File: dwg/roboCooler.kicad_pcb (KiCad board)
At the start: 2 copper layers, 139.7 x 137.2 mm, 44 parts, among them J1 CONN_02X25, J10 CONN_01X12, J11 CONN_01X12, J2 CONN_02X25, J3 CONN_01X04, J5 CONN_01X02, J7 CONN_01X02, J9 CONN_01X06, Q1 NMOS, Q2 NMOS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

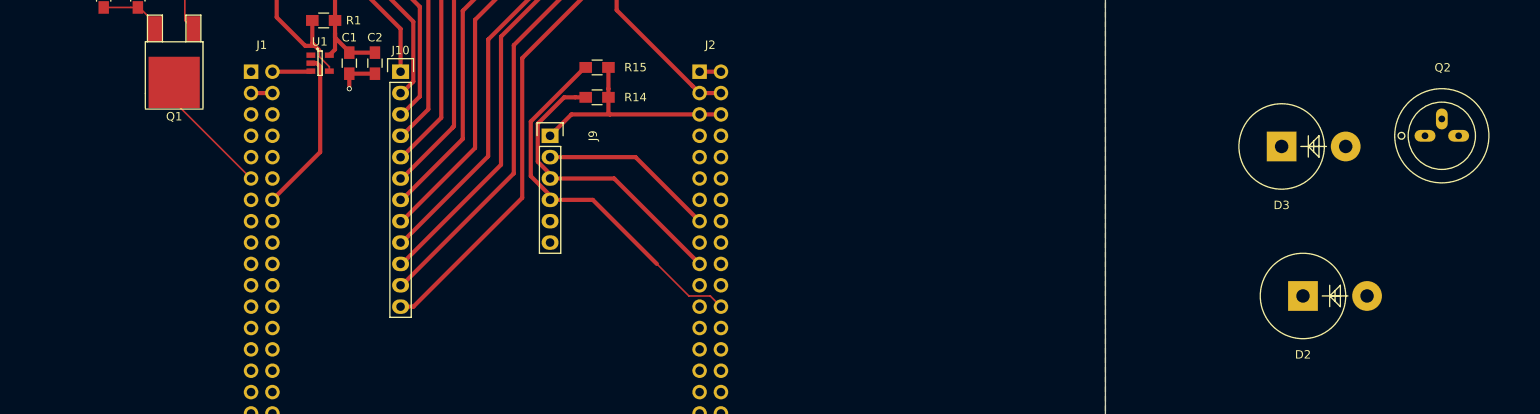
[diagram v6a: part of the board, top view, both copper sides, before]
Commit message: added pump parts to layout
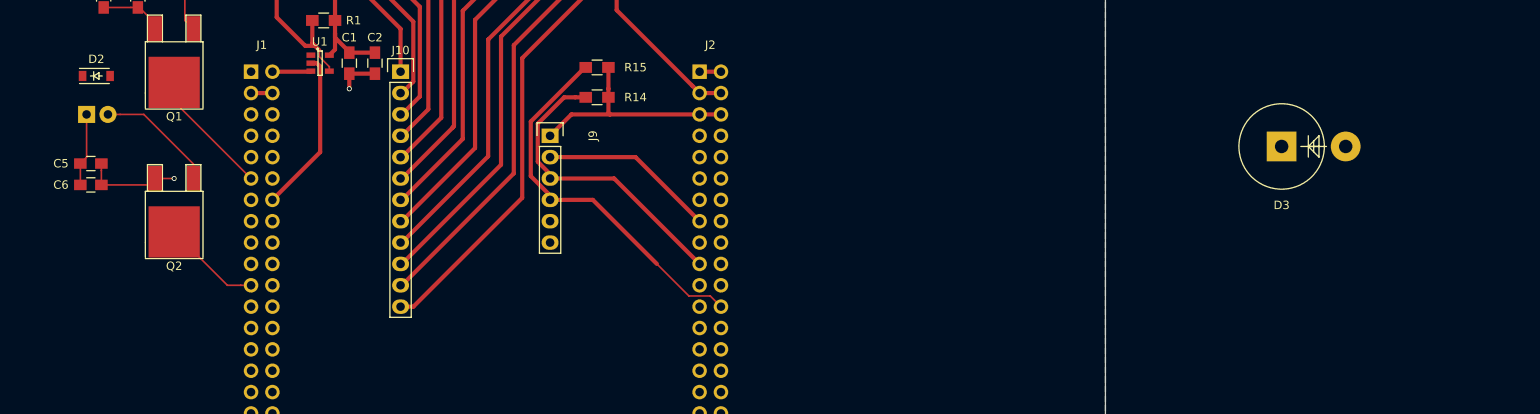
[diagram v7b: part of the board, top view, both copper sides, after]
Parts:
- added C5: .01UF, Capacitors_SMD:C_0805_HandSoldering, F.Cu at (44.5, 51.6)
- added C6: 1UF, Capacitors_SMD:C_0805_HandSoldering, F.Cu at (44.5, 54.1)
- added J4: CONN_01X02, Socket_Strips:Socket_Strip_Angled_1x02, B.Cu at (43.9, 45.7)
- D2: value D_Schottky_Small -> BAT42; footprint Diodes_ThroughHole:Diode_P600_Vertical_AnodeUp -> Diodes_SMD:SOD-123
- Q2: footprint Transistors_OldSowjetAera:OldSowjetaera_Transistor_Type-II_BigPads -> TO_SOT_Packages_SMD:TO-252-2Lead
- moved Q2 150.8 mm to (54.4, 53.3), turned to 180 degrees
- moved D2 145.9 mm to (45.1, 41.1)
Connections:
- J1 pad 21: Net-(J1-Pad21) -> PUMP
- J2 pad 25: PUMP -> Net-(J2-Pad25)
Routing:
- net Net-(D2-Pad2): track 0.00 -> 14.3 mm
- net PUMP: track 0.00 -> 12.7 mm
- net POWER_GND: track 19.8 -> 31.3 mm, vias 1 -> 2
- net +12V: track 11.3 -> 20.0 mm

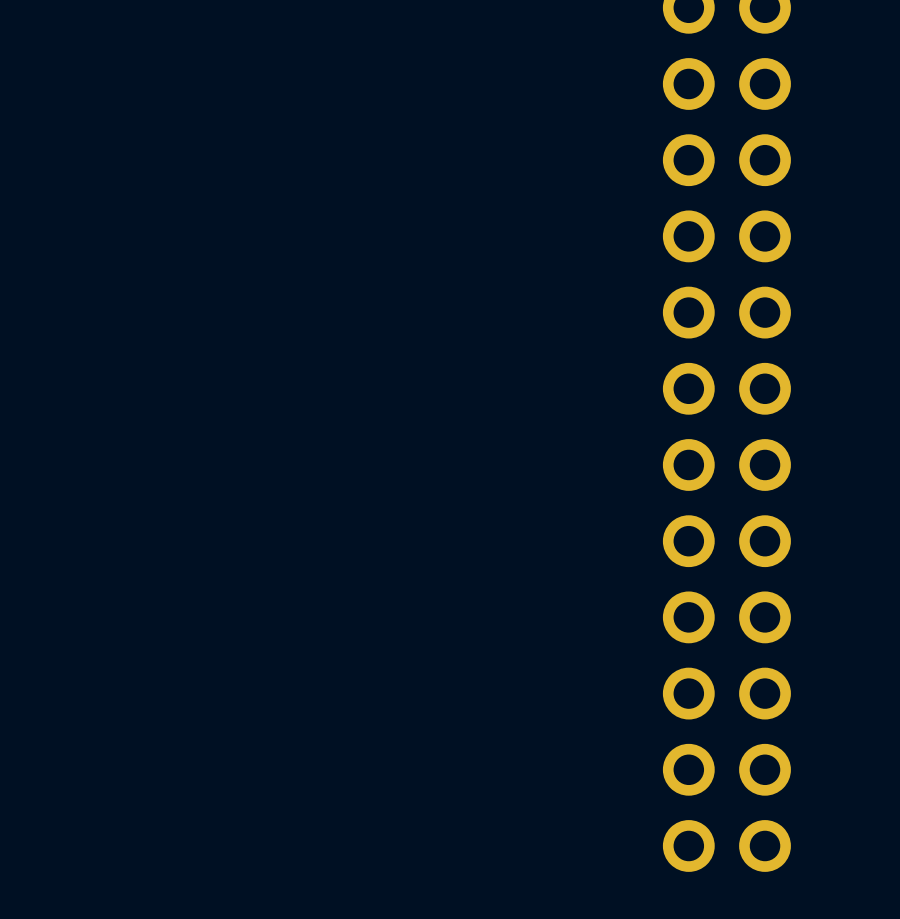
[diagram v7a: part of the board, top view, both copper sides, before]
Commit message: added hall sensors to layout
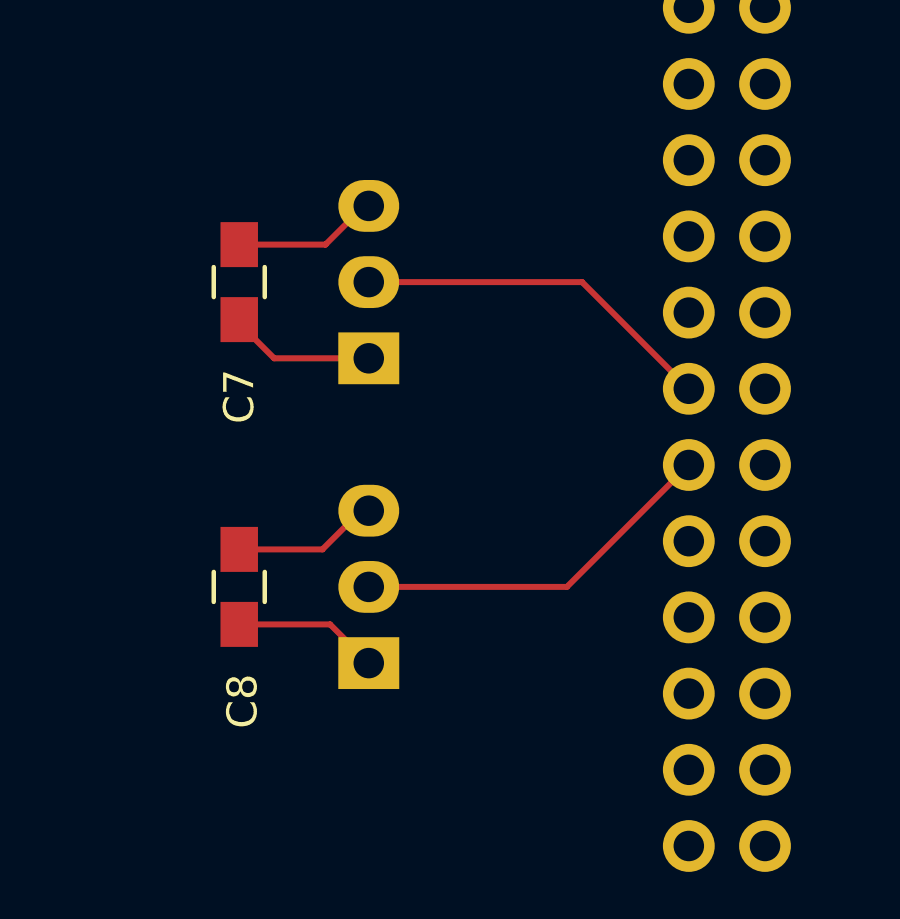
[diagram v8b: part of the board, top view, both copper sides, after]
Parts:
- added C7: .1UF, Capacitors_SMD:C_0805_HandSoldering, F.Cu at (48.5, 82.8)
- added C8: .1UF, Capacitors_SMD:C_0805_HandSoldering, F.Cu at (48.5, 93.0)
- added P1: CONN_01X03, Socket_Strips:Socket_Strip_Angled_1x03, B.Cu at (52.8, 85.3)
- added P2: CONN_01X03, Socket_Strips:Socket_Strip_Angled_1x03, B.Cu at (52.8, 95.5)
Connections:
- J1 pad 35: HALL_1 -> Net-(J1-Pad35)
- J1 pad 36: HALL_2 -> Net-(J1-Pad36)
- J1 pad 37: Net-(J1-Pad37) -> HALL_1
- J1 pad 39: Net-(J1-Pad39) -> HALL_2
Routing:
- net HALL_2: track 0.00 -> 12.4 mm
- net HALL_1: track 0.00 -> 12.1 mm
- net +5V: track 78.8 -> 88.6 mm
- net POWER_GND: track 31.3 -> 41.0 mm
